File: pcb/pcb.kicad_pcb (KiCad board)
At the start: 2 copper layers, 43.2 x 132.1 mm, 50 parts, among them J1 Barrel_Jack_Switch, J2 Conn_02x05_Odd_Even, J3 Conn_02x05_Odd_Even, Q1 RQ5P010SN, Q2 IRLML6244, SW1 SW_SPST, SW2 SW_SPST, SW3 SW_SPST, U1 L7805, U2 MCP1406/07, U3 MAX6921AWI, U4 MCP7940N-xSN, U5 Pico, Y1 32.768KHZ

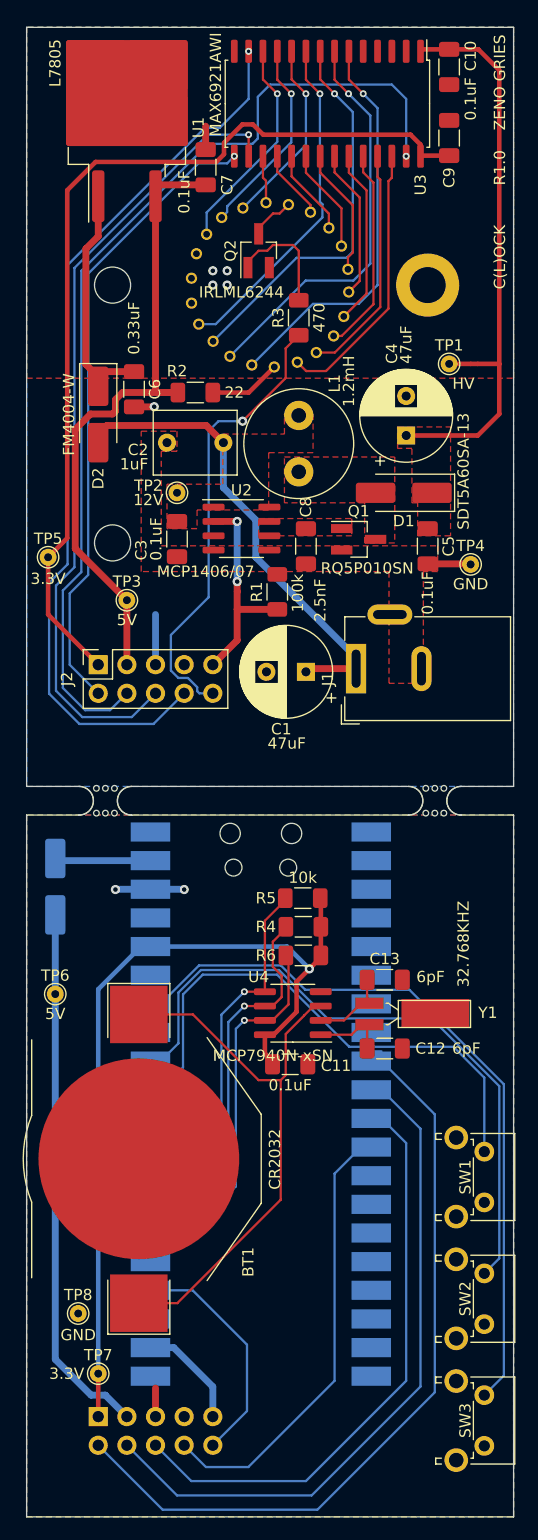
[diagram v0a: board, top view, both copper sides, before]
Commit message: updated pcb to R1.1
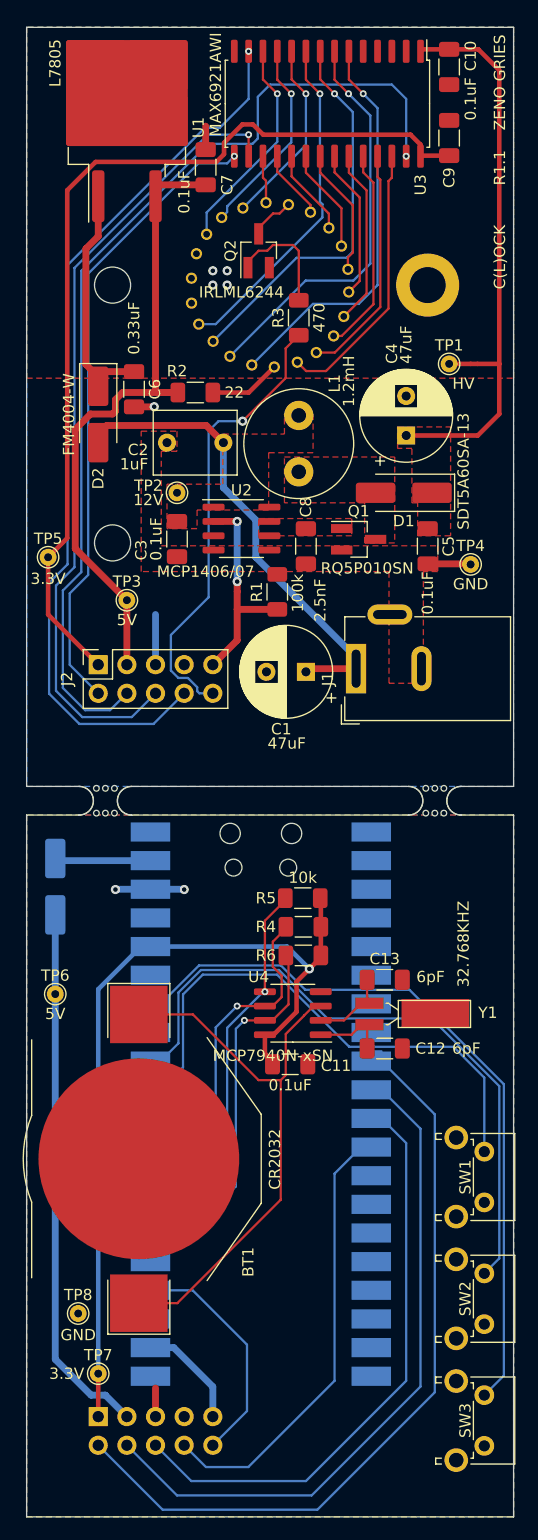
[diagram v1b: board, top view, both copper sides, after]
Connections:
- U5 pad 26: /SCL -> /SDA
- U5 pad 27: /SDA -> /SCL
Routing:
- net /SCL: track 33.9 -> 31.7 mm
- net /SDA: track 33.0 -> 34.6 mm
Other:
- board text added: "C(L)OCK R1.1 ZENO GRIES"
- board text removed: "C(L)OCK R1.0 ZENO GRIES"
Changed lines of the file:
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@@
       (net 15 "/MFP") (pinfunction "GPIO19") (pintype "bidirectional"))
     (pad "26" smd rect (at 8.89 -11.43 180) (size 3.5 1.7) (drill (offset 0.9 0)) (layers "B.Cu" "B.Mask")
-      (net 13 "/SCL") (pinfunction "GPIO20") (pintype "bidirectional"))
+      (net 14 "/SDA") (pinfunction "GPIO20") (pintype "bidirectional"))
     (pad "27" smd rect (at 8.89 -8.89 180) (size 3.5 1.7) (drill (offset 0.9 0)) (layers "B.Cu" "B.Mask")
-      (net 14 "/SDA") (pinfunction "GPIO21") (pintype "bidirectional"))
+      (net 13 "/SCL") (pinfunction "GPIO21") (pintype "bidirectional"))
     (pad "28" smd rect (at 8.89 -6.35 180) (size 3.5 1.7) (drill (offset 0.9 0)) (layers "B.Cu" "B.Mask")
       (net 81 "unconnected-(U5-GND-Pad28)") (pinfunction "GND") (pintype "power_in"))
@@
   (gr_rect (start 107.75 100.675) (end 153.75 176.675)
     (stroke (width 0.15) (type default)) (fill none) (layer "User.2"))
-  (gr_text "C(L)OCK		R1.0	ZENO GRIES" (at 151.765 34.925 90) (layer "F.SilkS")
+  (gr_text "C(L)OCK		R1.1	ZENO GRIES" (at 151.765 34.925 90) (layer "F.SilkS")
     (effects (font (size 1 1) (thickness 0.15)) (justify right bottom))
   )
@@
   (segment (start 131.038842 121.0762) (end 131.832 120.283042) (width 0.2032) (layer "F.Cu") (net 13))
   (segment (start 131.049 115.3742) (end 132.207 114.2162) (width 0.2032) (layer "F.Cu") (net 13))
-  (segment (start 128.524 121.0762) (end 130.349 121.0762) (width 0.2032) (layer "F.Cu") (net 13))
   (segment (start 131.049 117.587) (end 131.049 115.3742) (width 0.2032) (layer "F.Cu") (net 13))
+  (segment (start 127.883437 121.0762) (end 130.349 121.0762) (width 0.2032) (layer "F.Cu") (net 13))
   (segment (start 131.832 118.37) (end 131.049 117.587) (width 0.2032) (layer "F.Cu") (net 13))
   (segment (start 132.207 114.2162) (end 132.207 114.046) (width 0.2032) (layer "F.Cu") (net 13))
-  (via (at 128.524 121.0762) (size 0.6096) (drill 0.3048) (layers "F.Cu" "B.Cu") (net 13))
-  (segment (start 127.1016 135.1984) (end 121.1 141.2) (width 0.2032) (layer "B.Cu") (net 13))
-  (segment (start 127.1016 122.4986) (end 127.1016 135.1984) (width 0.2032) (layer "B.Cu") (net 13))
-  (segment (start 128.524 121.0762) (end 127.1016 122.4986) (width 0.2032) (layer "B.Cu") (net 13))
+  (via (at 127.883437 121.0762) (size 0.6096) (drill 0.3048) (layers "F.Cu" "B.Cu") (net 13))
+  (segment (start 127.883437 121.0762) (end 125.984 122.975637) (width 0.2032) (layer "B.Cu") (net 13))
+  (segment (start 125.984 122.975637) (end 125.984 133.776) (width 0.2032) (layer "B.Cu") (net 13))
+  (segment (start 125.984 133.776) (end 121.1 138.66) (width 0.2032) (layer "B.Cu") (net 13))
   (segment (start 130.349 119.8062) (end 130.349 113.509742) (width 0.2032) (layer "F.Cu") (net 14))
-  (segment (start 128.524 119.8062) (end 130.349 119.8062) (width 0.2032) (layer "F.Cu") (net 14))
   (segment (start 130.349 113.509742) (end 132.155 111.703742) (width 0.2032) (layer "F.Cu") (net 14))
   (segment (start 132.155 111.703742) (end 132.155 111.506) (width 0.2032) (layer "F.Cu") (net 14))
   (segment (start 132.155 111.70834) (end 132.155 111.506) (width 0.2032) (layer "F.Cu") (net 14))
-  (via (at 128.524 119.8062) (size 0.6096) (drill 0.3048) (layers "F.Cu" "B.Cu") (net 14))
-  (segment (start 126.492 121.8382) (end 126.492 133.268) (width 0.2032) (layer "B.Cu") (net 14))
-  (segment (start 128.524 119.8062) (end 126.492 121.8382) (width 0.2032) (layer "B.Cu") (net 14))
-  (segment (start 126.492 133.268) (end 121.1 138.66) (width 0.2032) (layer "B.Cu") (net 14))
+  (via (at 130.349 119.8062) (size 0.6096) (drill 0.3048) (layers "F.Cu" "B.Cu") (net 14))
+  (segment (start 130.201895 119.8062) (end 130.349 119.8062) (width 0.2032) (layer "B.Cu") (net 14))
+  (segment (start 127 135.3) (end 127 123.008095) (width 0.2032) (layer "B.Cu") (net 14))
+  (segment (start 127 123.008095) (end 130.201895 119.8062) (width 0.2032) (layer "B.Cu") (net 14))
+  (segment (start 121.1 141.2) (end 127 135.3) (width 0.2032) (layer "B.Cu") (net 14))
   (segment (start 131.024747 122.3462) (end 132.4416 120.929347) (width 0.2032) (layer "F.Cu") (net 15))
   (segment (start 132.4416 116.8206) (end 132.207 116.586) (width 0.2032) (layer "F.Cu") (net 15))

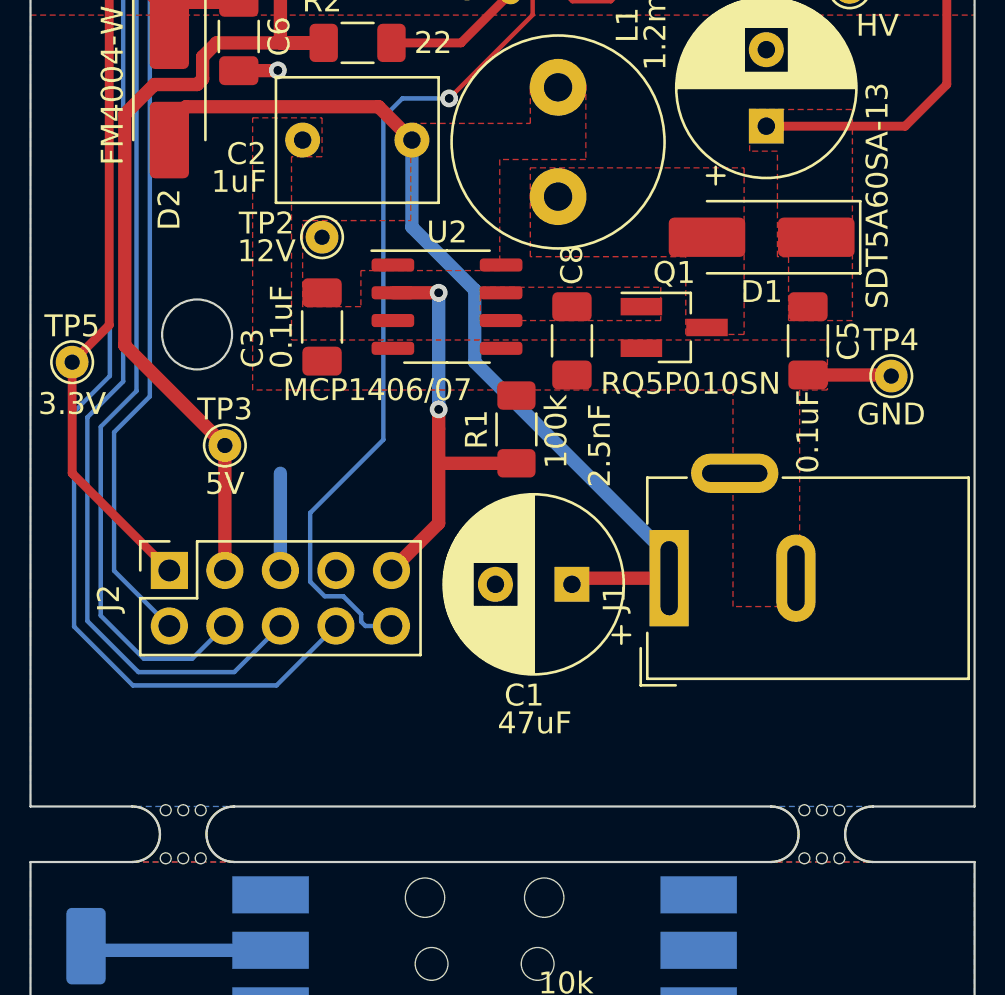
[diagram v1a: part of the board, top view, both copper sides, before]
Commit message: added resettable fuse
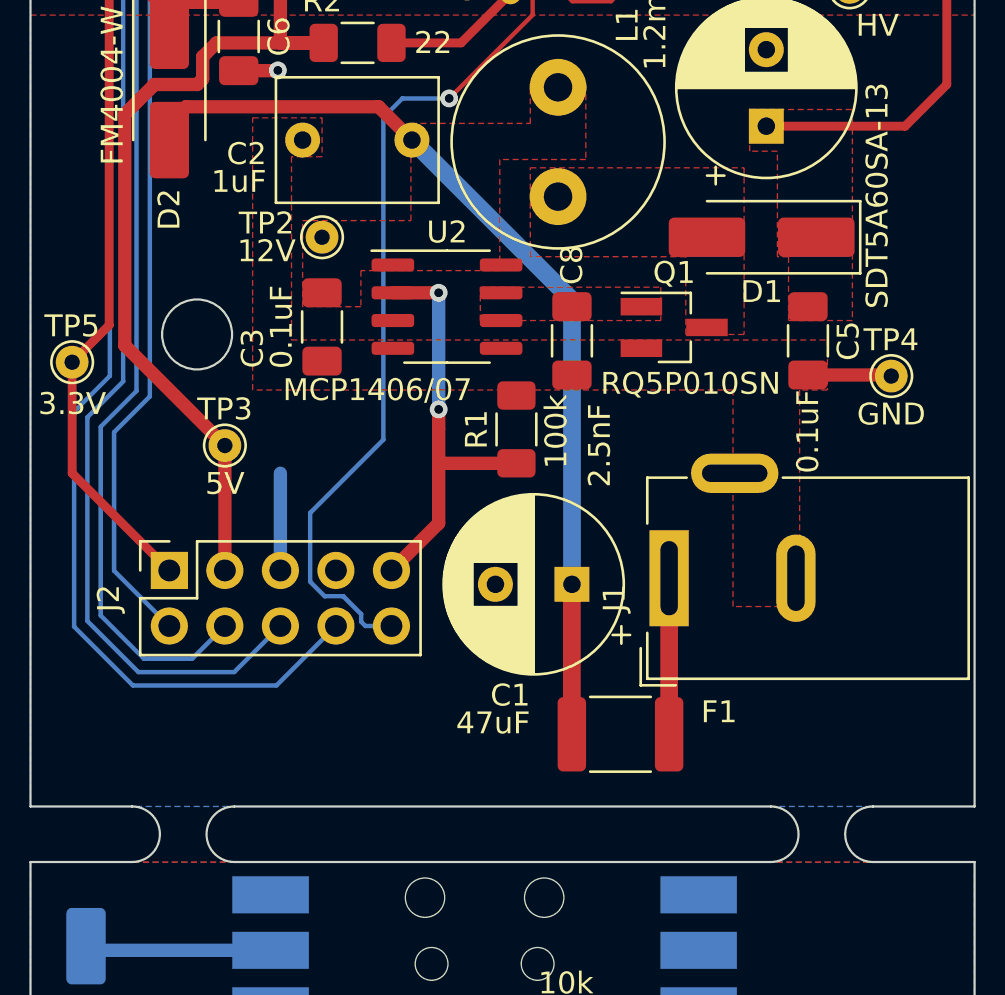
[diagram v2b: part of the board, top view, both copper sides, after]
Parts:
- removed mouse-bite-2.54mm-slot (x2): VAL**, Panelization:mouse-bite-2.54mm-slot
- added F1: Polyfuse, Fuse:Fuse_1812_4532Metric_Pad1.30x3.40mm_HandSolder, F.Cu at (136.2, 98.3)
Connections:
- J1 pad 1: +12V -> Net-(F1-Pad1)
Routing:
- net Net-(F1-Pad1): track 0.00 -> 8.13 mm
- net +12V: track 42.3 -> 43.4 mm
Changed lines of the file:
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@@
   (net 87 "unconnected-(J3-Pin_7-Pad7)")
   (net 88 "unconnected-(U5-GPIO22-Pad29)")
+  (net 89 "Net-(F1-Pad1)")
   (footprint "Button_Switch_THT:SW_Tactile_SPST_Angled_PTS645Vx83-2LFS" (layer "F.Cu")
     (at 149.8025 144.78 -90)
@@
       (net 6 "+5V") (pinfunction "1") (pintype "passive"))
   )
-  (footprint "Panelization:mouse-bite-2.54mm-slot" (layer "F.Cu")
-    (at 145.415 102.87)
-    (attr through_hole)
-    (fp_text reference "mouse-bite-2.54mm-slot" (at 0 -2) (layer "F.SilkS") hide
-        (effects (font (size 1 1) (thickness 0.2)))
-    )
-    (fp_text value "VAL**" (at 0 2.1) (layer "F.SilkS") hide
-        (effects (font (size 1 1) (thickness 0.2)))
-    )
-    (fp_arc (start -2.33 -1.27) (mid -1.06 0) (end -2.33 1.27)
-      (stroke (width 0.1) (type solid)) (layer "F.SilkS"))
-    (fp_arc (start 2.33 1.27) (mid 1.06 0) (end 2.33 -1.27)
-      (stroke (width 0.1) (type solid)) (layer "F.SilkS"))
-    (fp_circle (center -2.33 0) (end -2.27 0)
-      (stroke (width 0.05) (type solid)) (fill none) (layer "Dwgs.User"))
-    (fp_circle (center 2.33 0) (end 2.33 -0.06)
-      (stroke (width 0.05) (type solid)) (fill none) (layer "Dwgs.User"))
-    (fp_line (start -2.33 0) (end -2.33 0)
-      (stroke (width 2.54) (type solid)) (layer "Eco1.User"))
-    (fp_line (start 2.33 0) (end 2.33 0)
-      (stroke (width 2.54) (type solid)) (layer "Eco1.User"))
-    (pad "" np_thru_hole circle (at -0.8 -1.1) (size 0.5 0.5) (drill 0.5) (layers "F&B.Cu" "*.Mask"))
-    (pad "" np_thru_hole circle (at -0.8 1.1) (size 0.5 0.5) (drill 0.5) (layers "F&B.Cu" "*.Mask"))
-    (pad "" np_thru_hole circle (at 0 -1.1) (size 0.5 0.5) (drill 0.5) (layers "F&B.Cu" "*.Mask"))
-    (pad "" np_thru_hole circle (at 0 1.1) (size 0.5 0.5) (drill 0.5) (layers "F&B.Cu" "*.Mask"))
-    (pad "" np_thru_hole circle (at 0.8 -1.1) (size 0.5 0.5) (drill 0.5) (layers "F&B.Cu" "*.Mask"))
-    (pad "" np_thru_hole circle (at 0.8 1.1) (size 0.5 0.5) (drill 0.5) (layers "F&B.Cu" "*.Mask"))
-  )
   (footprint "Capacitor_SMD:C_1206_3216Metric_Pad1.33x1.80mm_HandSolder" (layer "F.Cu")
     (at 125.095 46.6975 90)
@@
     )
   )
+  (footprint "Fuse:Fuse_1812_4532Metric_Pad1.30x3.40mm_HandSolder" (layer "F.Cu")
+    (at 136.205 98.298 180)
+    (descr "Fuse SMD 1812 (4532 Metric), square (rectangular) end terminal, IPC_7351 nominal with elongated pad for handsoldering. (Body size source: https://www.nikhef.nl/pub/departments/mt/projects/detectorR_D/dtddice/ERJ2G.pdf), generated with kicad-footprint-generator")
+    (tags "fuse handsolder")
+    (property "Sheetfile" "pcb.kicad_sch")
+    (property "Sheetname" "")
+    (property "ki_description" "Resettable fuse, polymeric positive temperature coefficient")
+    (property "ki_keywords" "resettable fuse PTC PPTC polyfuse polyswitch")
+    (attr smd)
+    (fp_text reference "F1" (at -4.511 1.016) (layer "F.SilkS")
+        (effects (font (size 1 1) (thickness 0.15)))
+    )
+    (fp_text value "Polyfuse" (at 0 2.65) (layer "F.Fab")
+        (effects (font (size 1 1) (thickness 0.15)))
+    )
+    (fp_text user "${REFERENCE}" (at 0 0) (layer "F.Fab")
+        (effects (font (size 1 1) (thickness 0.15)))
+    )
+    (fp_line (start -1.386252 -1.71) (end 1.386252 -1.71)
+      (stroke (width 0.12) (type solid)) (layer "F.SilkS"))
+    (fp_line (start -1.386252 1.71) (end 1.386252 1.71)
+      (stroke (width 0.12) (type solid)) (layer "F.SilkS"))
+    (fp_line (start -3.12 -1.95) (end 3.12 -1.95)
+      (stroke (width 0.05) (type solid)) (layer "F.CrtYd"))
+    (fp_line (start -3.12 1.95) (end -3.12 -1.95)
+      (stroke (width 0.05) (type solid)) (layer "F.CrtYd"))
+    (fp_line (start 3.12 -1.95) (end 3.12 1.95)
+      (stroke (width 0.05) (type solid)) (layer "F.CrtYd"))
+    (fp_line (start 3.12 1.95) (end -3.12 1.95)
+      (stroke (width 0.05) (type solid)) (layer "F.CrtYd"))
+    (fp_line (start -2.25 -1.6) (end 2.25 -1.6)
+      (stroke (width 0.1) (type solid)) (layer "F.Fab"))
+    (fp_line (start -2.25 1.6) (end -2.25 -1.6)
+      (stroke (width 0.1) (type solid)) (layer "F.Fab"))
+    (fp_line (start 2.25 -1.6) (end 2.25 1.6)
+      (stroke (width 0.1) (type solid)) (layer "F.Fab"))
+    (fp_line (start 2.25 1.6) (end -2.25 1.6)
+      (stroke (width 0.1) (type solid)) (layer "F.Fab"))
+    (pad "1" smd roundrect (at -2.225 0 180) (size 1.3 3.4) (layers "F.Cu" "F.Paste" "F.Mask") (roundrect_rratio 0.192308)
+      (net 89 "Net-(F1-Pad1)") (pintype "passive"))
+    (pad "2" smd roundrect (at 2.225 0 180) (size 1.3 3.4) (layers "F.Cu" "F.Paste" "F.Mask") (roundrect_rratio 0.192308)
+      (net 3 "+12V") (pintype "passive"))
+    (model "${KICAD6_3DMODEL_DIR}/Fuse.3dshapes/Fuse_1812_4532Metric.wrl"
+      (offset (xyz 0 0 0))
+      (scale (xyz 1 1 1))
+      (rotate (xyz 0 0 0))
+    )
+  )
   (footprint "Button_Switch_THT:SW_Tactile_SPST_Angled_PTS645Vx83-2LFS" (layer "F.Cu")
     (at 149.8025 155.575 -90)
@@
     )
   )
-  (footprint "Panelization:mouse-bite-2.54mm-slot" (layer "F.Cu")
-    (at 116.205 102.87)
-    (attr through_hole)
-    (fp_text reference "mouse-bite-2.54mm-slot" (at 0 -2) (layer "F.SilkS") hide
-        (effects (font (size 1 1) (thickness 0.2)))
-    )
-    (fp_text value "VAL**" (at 0 2.1) (layer "F.SilkS") hide
-        (effects (font (size 1 1) (thickness 0.2)))
-    )
-    (fp_arc (start -2.33 -1.27) (mid -1.06 0) (end -2.33 1.27)
-      (stroke (width 0.1) (type solid)) (layer "F.SilkS"))
-    (fp_arc (start 2.33 1.27) (mid 1.06 0) (end 2.33 -1.27)
-      (stroke (width 0.1) (type solid)) (layer "F.SilkS"))
-    (fp_circle (center -2.33 0) (end -2.27 0)
-      (stroke (width 0.05) (type solid)) (fill none) (layer "Dwgs.User"))
-    (fp_circle (center 2.33 0) (end 2.33 -0.06)
-      (stroke (width 0.05) (type solid)) (fill none) (layer "Dwgs.User"))
-    (fp_line (start -2.33 0) (end -2.33 0)
-      (stroke (width 2.54) (type solid)) (layer "Eco1.User"))
-    (fp_line (start 2.33 0) (end 2.33 0)
-      (stroke (width 2.54) (type solid)) (layer "Eco1.User"))
-    (pad "" np_thru_hole circle (at -0.8 -1.1) (size 0.5 0.5) (drill 0.5) (layers "*.Cu" "*.Mask"))
-    (pad "" np_thru_hole circle (at -0.8 1.1) (size 0.5 0.5) (drill 0.5) (layers "*.Cu" "*.Mask"))
-    (pad "" np_thru_hole circle (at 0 -1.1) (size 0.5 0.5) (drill 0.5) (layers "*.Cu" "*.Mask"))
-    (pad "" np_thru_hole circle (at 0 1.1) (size 0.5 0.5) (drill 0.5) (layers "*.Cu" "*.Mask"))
-    (pad "" np_thru_hole circle (at 0.8 -1.1) (size 0.5 0.5) (drill 0.5) (layers "*.Cu" "*.Mask"))
-    (pad "" np_thru_hole circle (at 0.8 1.1) (size 0.5 0.5) (drill 0.5) (layers "*.Cu" "*.Mask"))
-  )
   (footprint "Battery:BatteryHolder_Keystone_3002_1x2032" (layer "F.Cu")
     (at 119.17 134.62 90)
@@
       (stroke (width 0.1) (type solid)) (layer "F.Fab"))
     (pad "1" thru_hole rect (at 0 0 90) (size 4.4 1.8) (drill oval 3.4 0.8) (layers "*.Cu" "*.Mask")
-      (net 3 "+12V") (pintype "passive"))
+      (net 89 "Net-(F1-Pad1)") (pintype "passive"))
     (pad "2" thru_hole oval (at 0 5.8 90) (size 4 1.8) (drill oval 3 0.8) (layers "*.Cu" "*.Mask")
       (net 2 "GND") (pintype "passive"))
@@
     (property "ki_keywords" "cap capacitor")
     (attr through_hole)
-    (fp_text reference "C1" (at 1.27 -5.08) (layer "F.SilkS")
+    (fp_text reference "C1" (at 1.905 -5.08) (layer "F.SilkS")
         (effects (font (size 1 1) (thickness 0.15)) (justify right))
     )
-    (fp_text value "47uF" (at 0 -6.35) (layer "F.SilkS")
+    (fp_text value "47uF" (at 1.905 -6.35) (layer "F.SilkS")
         (effects (font (size 1 1) (thickness 0.15)) (justify right))
     )
@@
   (segment (start 115.57 70.358) (end 115.57 71.12) (width 0.6096) (layer "F.Cu") (net 3))
   (segment (start 116.332 69.596) (end 115.57 70.358) (width 0.6096) (layer "F.Cu") (net 3))
+  (segment (start 133.98 91.445) (end 133.985 91.44) (width 0.6096) (layer "F.Cu") (net 3))
   (segment (start 125.142 69.596) (end 116.332 69.596) (width 0.6096) (layer "F.Cu") (net 3))
-  (segment (start 134.265 91.16) (end 138.43 91.16) (width 0.6096) (layer "F.Cu") (net 3))
-  (segment (start 138.43 91.16) (end 138.43 90.17) (width 0.6096) (layer "B.Cu") (net 3))
-  (segment (start 129.54 77.978) (end 126.666 75.104) (width 0.6096) (layer "B.Cu") (net 3))
-  (segment (start 126.666 75.104) (end 126.666 71.12) (width 0.6096) (layer "B.Cu") (net 3))
-  (segment (start 129.54 81.28) (end 129.54 77.978) (width 0.6096) (layer "B.Cu") (net 3))
-  (segment (start 138.43 90.17) (end 129.54 81.28) (width 0.6096) (layer "B.Cu") (net 3))
+  (segment (start 133.98 98.298) (end 133.98 91.445) (width 0.8128) (layer "F.Cu") (net 3))
+  (segment (start 133.985 91.44) (end 133.985 78.439) (width 0.8128) (layer "B.Cu") (net 3))
+  (segment (start 133.985 78.439) (end 126.666 71.12) (width 0.8128) (layer "B.Cu") (net 3))
   (segment (start 146.685 36.245) (end 144.32 36.245) (width 0.4064) (layer "F.Cu") (net 4))
   (segment (start 149.275 36.245) (end 146.685 36.245) (width 0.4064) (layer "F.Cu") (net 4))
@@
   (segment (start 129.794 52.072978) (end 129.794 52.602) (width 0.2032) (layer "F.Cu") (net 85))
   (segment (start 131.066978 50.8) (end 129.794 52.072978) (width 0.2032) (layer "F.Cu") (net 85))
+  (segment (start 138.43 91.16) (end 138.43 98.298) (width 0.8128) (layer "F.Cu") (net 89))
+  (segment (start 138.43 91.16) (end 138.43 90.17) (width 0.6096) (layer "B.Cu") (net 89))
   (zone (net 8) (net_name "GNDA") (layer "F.Cu") (hatch edge 0.5)
     (priority 7)
